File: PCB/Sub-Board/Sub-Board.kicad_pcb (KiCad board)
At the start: 4 copper layers, 50.5 x 113 mm, 200 parts, among them J1 Conn_02x08, J10 Type, J11 Power/I2C, J12 Address, J13 Power/I2C, J14 Address, J15 GPIO, J16 Type, J17 GPIO, J18 Type, J19 Power/I2C, J2 Conn_01x04_Pin, J20 Address, J21 Power/I2C, J22 Address, J23 GPIO, J24 Type, J25 GPIO, J26 Type, J27 Power/I2C, J28 Address, J29 Power/I2C, J3 Power/I2C, J30 Address, J31 GPIO, J32 Type, J33 GPIO, J34 Type, J4 Address, J5 Power/I2C, J6 Address, J7 GPIO, J8 Type, J9 GPIO, SW1 SW_DIP_x07, U1 TPS629210DRLR, U2 74HC165, U3 STM32F401VETx, U4 74HC165, U5 74HC165, U6 74HC165, U7 74HC165, Y1 26 MHz

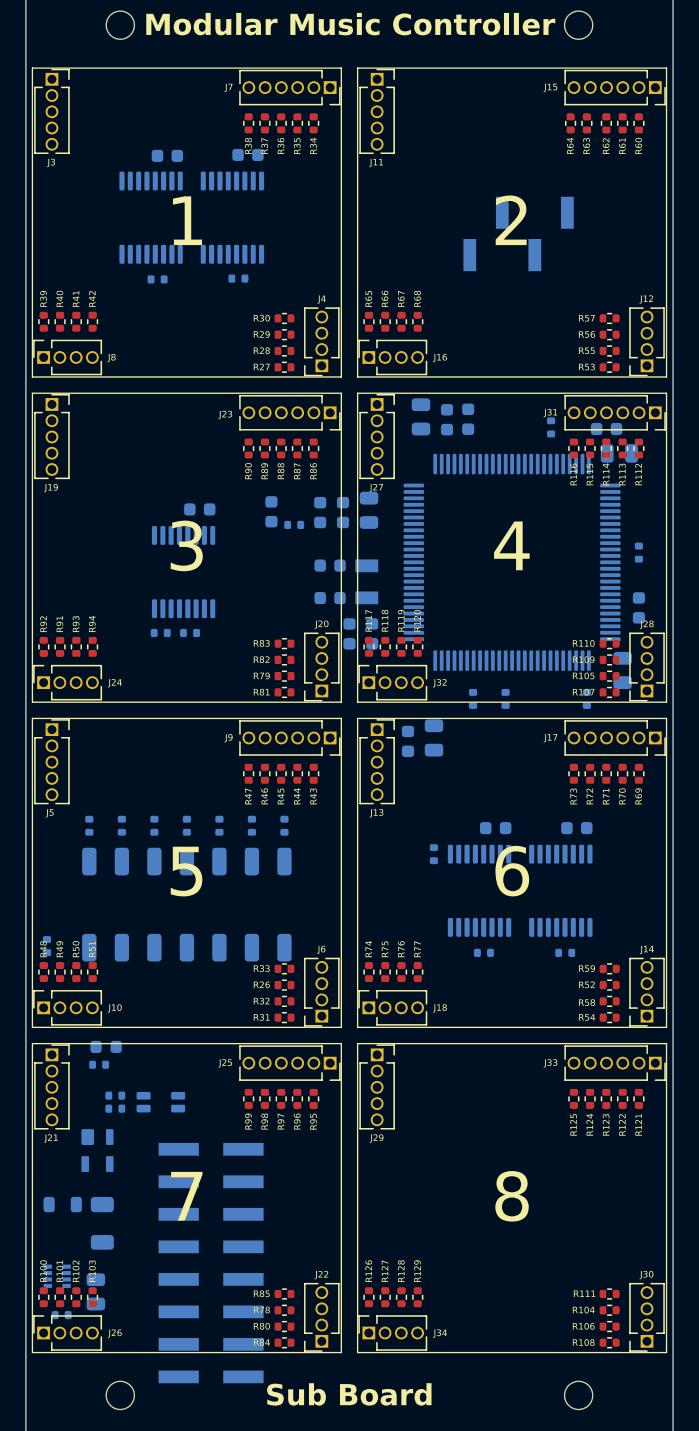
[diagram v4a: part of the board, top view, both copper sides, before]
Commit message: Sub Board PCB: Fix silkscreen size
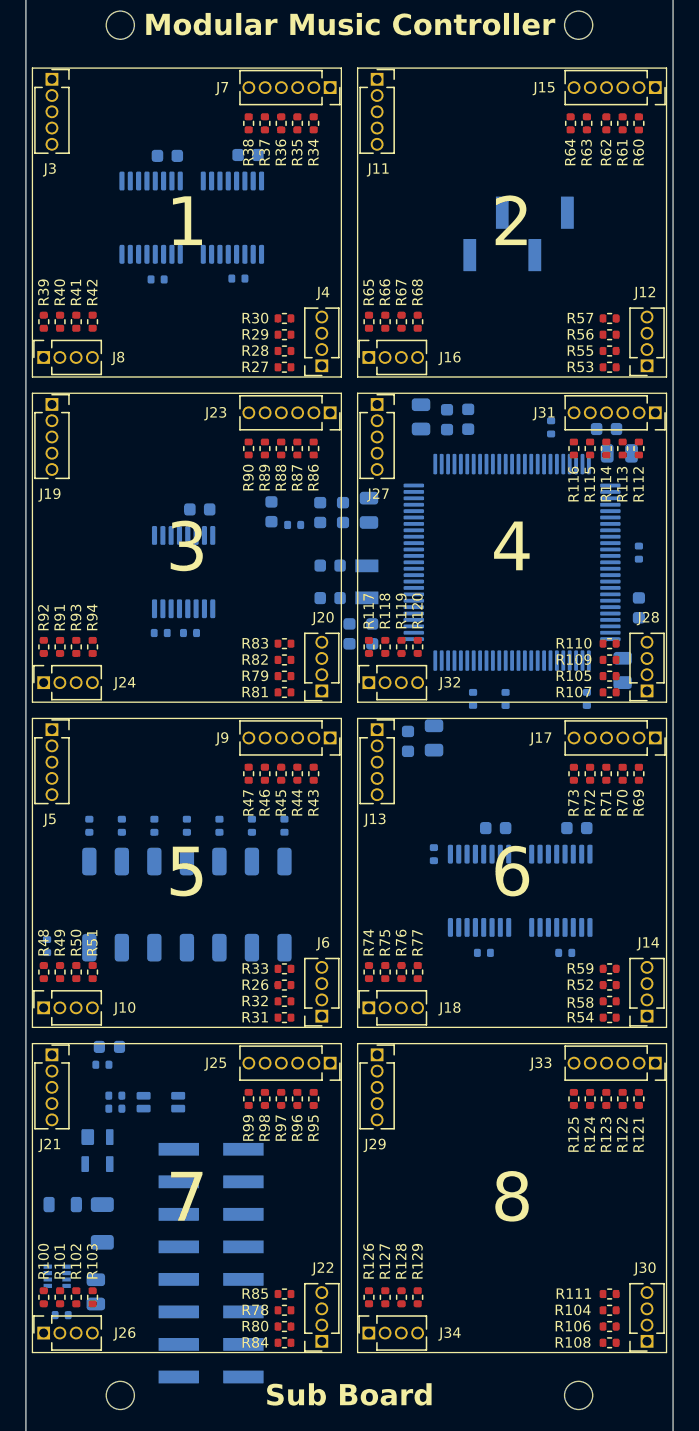
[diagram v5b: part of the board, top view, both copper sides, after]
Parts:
- moved FB1 0.26 mm to (108.2, 120.9)
- moved R4 0.26 mm to (107.7, 122.3)
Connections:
- net Net-(U1-MODE/S-CONF) renamed /Power Supply/MODE/S-CONF
- C14 pad 2: GND -> GNDD
- C17 pad 2: GND -> GNDD
- C21 pad 2: GND -> GNDD
- C24 pad 2: GND -> GNDD
- C3 pad 2: GND -> GNDD
- C4 pad 2: GND -> GNDD
- C5 pad 2: GND -> GNDD
- C6 pad 2: GND -> GNDD
- R10 pad 2: GND -> GNDD
- R100 pad 1: GND -> GNDD
- R101 pad 1: GND -> GNDD
- R102 pad 1: GND -> GNDD
- R103 pad 1: GND -> GNDD
- R109 pad 2: GND -> GNDD
- R11 pad 2: GND -> GNDD
- R110 pad 2: GND -> GNDD
- R111 pad 2: GND -> GNDD
- R112 pad 1: GND -> GNDD
- R113 pad 1: GND -> GNDD
- R114 pad 1: GND -> GNDD
- R115 pad 1: GND -> GNDD
- R116 pad 1: GND -> GNDD
- R117 pad 1: GND -> GNDD
- R118 pad 1: GND -> GNDD
- R119 pad 1: GND -> GNDD
- R12 pad 2: GND -> GNDD
- R120 pad 1: GND -> GNDD
- R121 pad 1: GND -> GNDD
- R122 pad 1: GND -> GNDD
- R123 pad 1: GND -> GNDD
- R124 pad 1: GND -> GNDD
- R125 pad 1: GND -> GNDD
- R126 pad 1: GND -> GNDD
- R127 pad 1: GND -> GNDD
- R128 pad 1: GND -> GNDD
- R129 pad 1: GND -> GNDD
- R24 pad 1: GND -> GNDD
- R27 pad 2: GND -> GNDD
- R28 pad 2: GND -> GNDD
- R29 pad 2: GND -> GNDD
- R30 pad 2: GND -> GNDD
- R31 pad 2: GND -> GNDD
- R32 pad 2: GND -> GNDD
- R33 pad 2: GND -> GNDD
- R34 pad 1: GND -> GNDD
- R35 pad 1: GND -> GNDD
- R36 pad 1: GND -> GNDD
- R37 pad 1: GND -> GNDD
- R38 pad 1: GND -> GNDD
- R39 pad 1: GND -> GNDD
- R40 pad 1: GND -> GNDD
- R41 pad 1: GND -> GNDD
- R42 pad 1: GND -> GNDD
- R43 pad 1: GND -> GNDD
- R44 pad 1: GND -> GNDD
- R45 pad 1: GND -> GNDD
- R46 pad 1: GND -> GNDD
- R47 pad 1: GND -> GNDD
- R48 pad 1: GND -> GNDD
- R49 pad 1: GND -> GNDD
- R50 pad 1: GND -> GNDD
- R51 pad 1: GND -> GNDD
- R55 pad 2: GND -> GNDD
- R56 pad 2: GND -> GNDD
- R57 pad 2: GND -> GNDD
- R58 pad 2: GND -> GNDD
- R59 pad 2: GND -> GNDD
- R6 pad 2: GND -> GNDD
- R60 pad 1: GND -> GNDD
- R61 pad 1: GND -> GNDD
- R62 pad 1: GND -> GNDD
- R63 pad 1: GND -> GNDD
- R64 pad 1: GND -> GNDD
- R65 pad 1: GND -> GNDD
- R66 pad 1: GND -> GNDD
- R67 pad 1: GND -> GNDD
- R68 pad 1: GND -> GNDD
- R69 pad 1: GND -> GNDD
- R7 pad 2: GND -> GNDD
- R70 pad 1: GND -> GNDD
- R71 pad 1: GND -> GNDD
- R72 pad 1: GND -> GNDD
- R73 pad 1: GND -> GNDD
- R74 pad 1: GND -> GNDD
- R75 pad 1: GND -> GNDD
- R76 pad 1: GND -> GNDD
- R77 pad 1: GND -> GNDD
- R8 pad 2: GND -> GNDD
- R81 pad 2: GND -> GNDD
- R82 pad 2: GND -> GNDD
- R83 pad 2: GND -> GNDD
- R84 pad 2: GND -> GNDD
- R85 pad 2: GND -> GNDD
- R86 pad 1: GND -> GNDD
- R87 pad 1: GND -> GNDD
- R88 pad 1: GND -> GNDD
- R89 pad 1: GND -> GNDD
- R9 pad 2: GND -> GNDD
- R90 pad 1: GND -> GNDD
- R91 pad 1: GND -> GNDD
- R92 pad 1: GND -> GNDD
- R93 pad 1: GND -> GNDD
- R94 pad 1: GND -> GNDD
- R95 pad 1: GND -> GNDD
- R96 pad 1: GND -> GNDD
- R97 pad 1: GND -> GNDD
- R98 pad 1: GND -> GNDD
- R99 pad 1: GND -> GNDD
- U2 pad 10: GND -> GNDD
- U2 pad 15: GND -> GNDD
- U4 pad 15: GND -> GNDD
- U5 pad 15: GND -> GNDD
- U6 pad 15: GND -> GNDD
- U7 pad 15: GND -> GNDD

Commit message: Sub Board PCB: Routing (wip)
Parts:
- moved R91 1.27 mm to (103.1, 89.7)
- moved R92 1.27 mm to (104.4, 89.7)
- moved R1 1.02 mm to (108.7, 124.7)
- moved R2 1.02 mm to (108.7, 125.7)
- turned R3 to 0 degrees
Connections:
- C14 pad 2: GNDD -> GND
- C17 pad 2: GNDD -> GND
- C21 pad 2: GNDD -> GND
- C24 pad 2: GNDD -> GND
- C3 pad 2: GNDD -> GND
- C4 pad 2: GNDD -> GND
- C5 pad 2: GNDD -> GND
- C6 pad 2: GNDD -> GND
- L1 pad 2: /STM32-MCU/SystemBus.Clock -> /STM32-MCU/SystemBus.Data
- L1 pad 3: /STM32-MCU/SystemBus.Data -> /STM32-MCU/SystemBus.Clock
- R1 pad 2: Net-(L1-Pad1) -> Net-(L1-Pad4)
- R10 pad 2: GNDD -> GND
- R100 pad 1: GNDD -> GND
- R101 pad 1: GNDD -> GND
- R102 pad 1: GNDD -> GND
- R103 pad 1: GNDD -> GND
- R109 pad 2: GNDD -> GND
- R11 pad 2: GNDD -> GND
- R110 pad 2: GNDD -> GND
- R111 pad 2: GNDD -> GND
- R112 pad 1: GNDD -> GND
- R113 pad 1: GNDD -> GND
- R114 pad 1: GNDD -> GND
- R115 pad 1: GNDD -> GND
- R116 pad 1: GNDD -> GND
- R117 pad 1: GNDD -> GND
- R118 pad 1: GNDD -> GND
- R119 pad 1: GNDD -> GND
- R12 pad 2: GNDD -> GND
- R120 pad 1: GNDD -> GND
- R121 pad 1: GNDD -> GND
- R122 pad 1: GNDD -> GND
- R123 pad 1: GNDD -> GND
- R124 pad 1: GNDD -> GND
- R125 pad 1: GNDD -> GND
- R126 pad 1: GNDD -> GND
- R127 pad 1: GNDD -> GND
- R128 pad 1: GNDD -> GND
- R129 pad 1: GNDD -> GND
- R2 pad 2: Net-(L1-Pad4) -> Net-(L1-Pad1)
- R24 pad 1: GNDD -> GND
- R27 pad 2: GNDD -> GND
- R28 pad 2: GNDD -> GND
- R29 pad 2: GNDD -> GND
- R30 pad 2: GNDD -> GND
- R31 pad 2: GNDD -> GND
- R32 pad 2: GNDD -> GND
- R33 pad 2: GNDD -> GND
- R34 pad 1: GNDD -> GND
- R35 pad 1: GNDD -> GND
- R36 pad 1: GNDD -> GND
- R37 pad 1: GNDD -> GND
- R38 pad 1: GNDD -> GND
- R39 pad 1: GNDD -> GND
- R40 pad 1: GNDD -> GND
- R41 pad 1: GNDD -> GND
- R42 pad 1: GNDD -> GND
- R43 pad 1: GNDD -> GND
- R44 pad 1: GNDD -> GND
- R45 pad 1: GNDD -> GND
- R46 pad 1: GNDD -> GND
- R47 pad 1: GNDD -> GND
- R48 pad 1: GNDD -> GND
- R49 pad 1: GNDD -> GND
- R50 pad 1: GNDD -> GND
- R51 pad 1: GNDD -> GND
- R55 pad 2: GNDD -> GND
- R56 pad 2: GNDD -> GND
- R57 pad 2: GNDD -> GND
- R58 pad 2: GNDD -> GND
- R59 pad 2: GNDD -> GND
- R6 pad 2: GNDD -> GND
- R60 pad 1: GNDD -> GND
- R61 pad 1: GNDD -> GND
- R62 pad 1: GNDD -> GND
- R63 pad 1: GNDD -> GND
- R64 pad 1: GNDD -> GND
- R65 pad 1: GNDD -> GND
- R66 pad 1: GNDD -> GND
- R67 pad 1: GNDD -> GND
- R68 pad 1: GNDD -> GND
- R69 pad 1: GNDD -> GND
- R7 pad 2: GNDD -> GND
- R70 pad 1: GNDD -> GND
- R71 pad 1: GNDD -> GND
- R72 pad 1: GNDD -> GND
- R73 pad 1: GNDD -> GND
- R74 pad 1: GNDD -> GND
- R75 pad 1: GNDD -> GND
- R76 pad 1: GNDD -> GND
- R77 pad 1: GNDD -> GND
- R8 pad 2: GNDD -> GND
- R81 pad 2: GNDD -> GND
- R82 pad 2: GNDD -> GND
- R83 pad 2: GNDD -> GND
- R84 pad 2: GNDD -> GND
- R85 pad 2: GNDD -> GND
- R86 pad 1: GNDD -> GND
- R87 pad 1: GNDD -> GND
- R88 pad 1: GNDD -> GND
- R89 pad 1: GNDD -> GND
- R9 pad 2: GNDD -> GND
- R90 pad 1: GNDD -> GND
- R91 pad 1: GNDD -> GND
- R92 pad 1: GNDD -> GND
- R93 pad 1: GNDD -> GND
- R94 pad 1: GNDD -> GND
- R95 pad 1: GNDD -> GND
- R96 pad 1: GNDD -> GND
- R97 pad 1: GNDD -> GND
- R98 pad 1: GNDD -> GND
- R99 pad 1: GNDD -> GND
- U2 pad 10: GNDD -> GND
- U2 pad 15: GNDD -> GND
- U4 pad 15: GNDD -> GND
- U5 pad 15: GNDD -> GND
- U6 pad 15: GNDD -> GND
- U7 pad 15: GNDD -> GND
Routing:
- net GND: track 0.00 -> 136.8 mm, vias 0 -> 42
- net /Board Address/+3.3V Digital: track 0.00 -> 25.8 mm, vias 0 -> 10
- net /System Bus/+5V: track 0.00 -> 16.4 mm
- net /System Bus/SystemBus-Data: track 0.00 -> 15.8 mm
- net /System Bus/SystemBus-Clock: track 0.00 -> 14.5 mm
- net /System Bus/-12V: track 0.00 -> 5.05 mm
- net /System Bus/+12V: track 0.00 -> 5.05 mm
- net Net-(U1-SW): track 0.00 -> 4.90 mm
- net /Power Supply/MODE/S-CONF: track 0.00 -> 2.65 mm
- net /STM32-MCU/Slot7.Addr2: track 0.00 -> 2.46 mm
- net /STM32-MCU/Slot7.Addr1: track 0.00 -> 2.46 mm
- net /STM32-MCU/Slot7.Addr0: track 0.00 -> 2.46 mm
- net /STM32-MCU/Slot4.Addr2: track 0.00 -> 2.46 mm
- net /STM32-MCU/Slot1.Addr2: track 0.00 -> 2.46 mm
- net /STM32-MCU/Slot1.Addr1: track 0.00 -> 2.46 mm
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
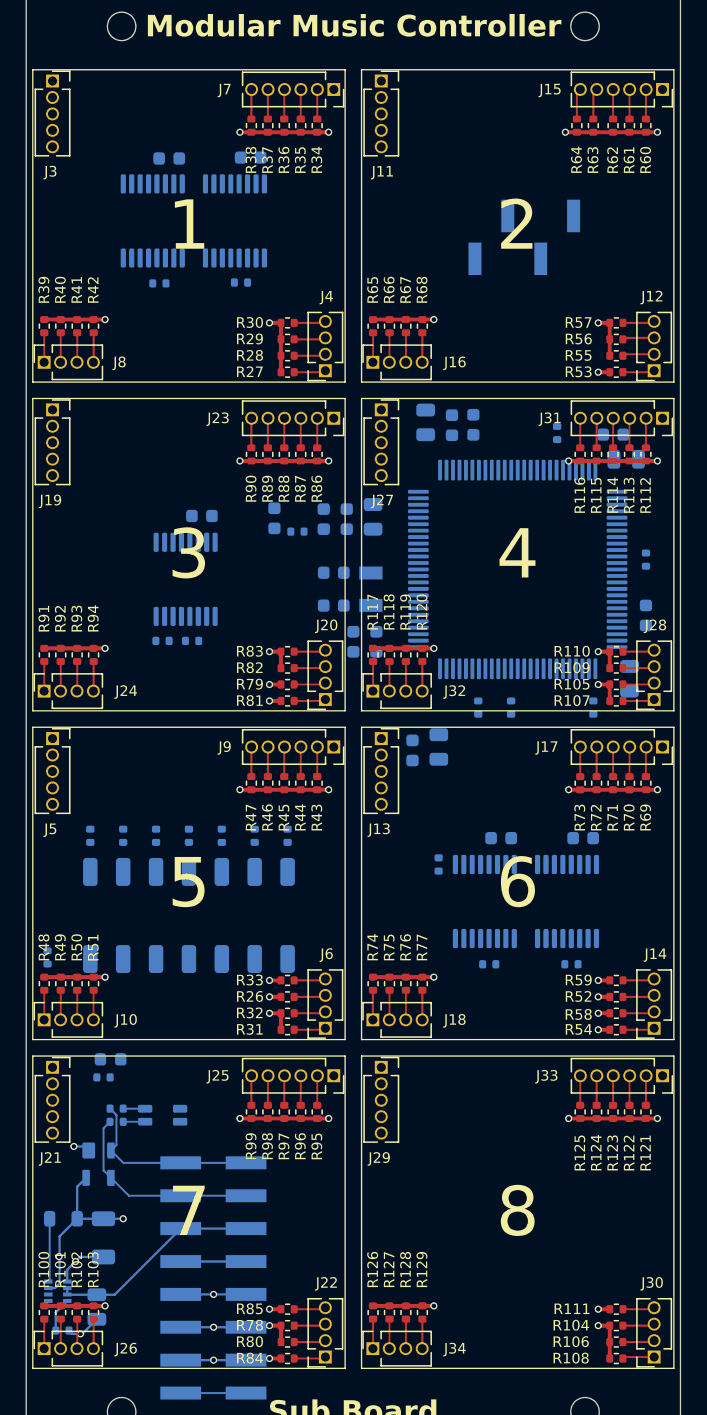
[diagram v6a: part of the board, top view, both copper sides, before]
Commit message: Sub Board PCB: Power routing
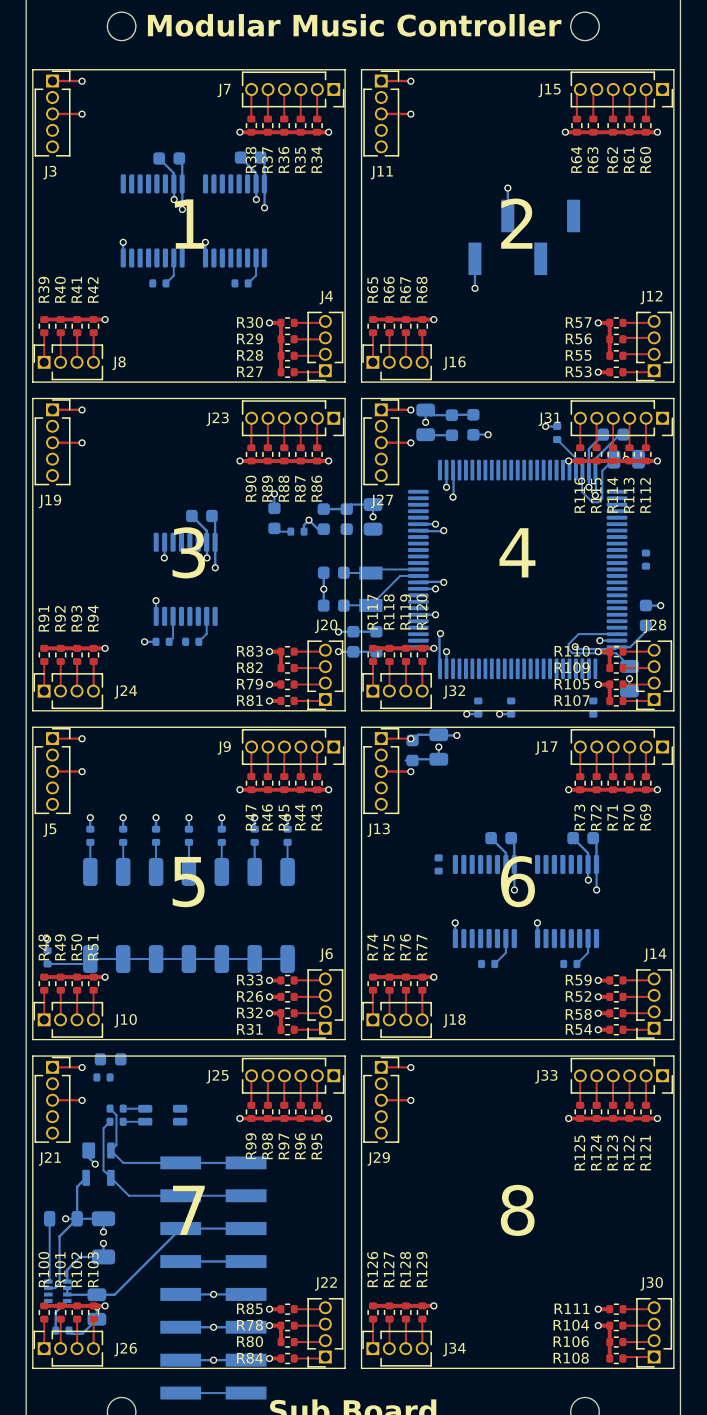
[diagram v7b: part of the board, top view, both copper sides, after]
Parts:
- moved R22 0.09 mm to (137.4, 113.5)
- moved R19 0.09 mm to (143.8, 113.5)
- moved R15 0.08 mm to (118.4, 61.0)
- moved R14 0.07 mm to (114.6, 88.6)
- moved R13 0.07 mm to (112.3, 88.6)
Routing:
- net GND: track 136.8 -> 227.4 mm, vias 42 -> 85
- net /Board Address/+3.3V Digital: track 25.8 -> 103.6 mm, vias 10 -> 39
- net Net-(R5-Pad2): track 0.00 -> 18.7 mm
- net /STM32-MCU/VCAP2: track 0.00 -> 9.78 mm
- net /STM32-MCU/VCAP1: track 0.00 -> 7.11 mm
- net /STM32-MCU/PH0: track 0.00 -> 6.71 mm
- net /STM32-MCU/PH1: track 0.00 -> 5.88 mm
- net /STM32-MCU/SlotBus.Data: track 0.00 -> 2.96 mm
- net Net-(U7-CP): track 0.00 -> 2.32 mm
- net Net-(U6-CP): track 0.00 -> 2.32 mm
- net /Board Address/BoardAddress6: track 0.00 -> 2.29 mm
- net /Board Address/BoardAddress5: track 0.00 -> 2.28 mm
- net /Board Address/BoardAddress4: track 0.00 -> 2.28 mm
- net /Board Address/BoardAddress3: track 0.00 -> 2.28 mm
- net /Board Address/BoardAddress2: track 0.00 -> 2.28 mm
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
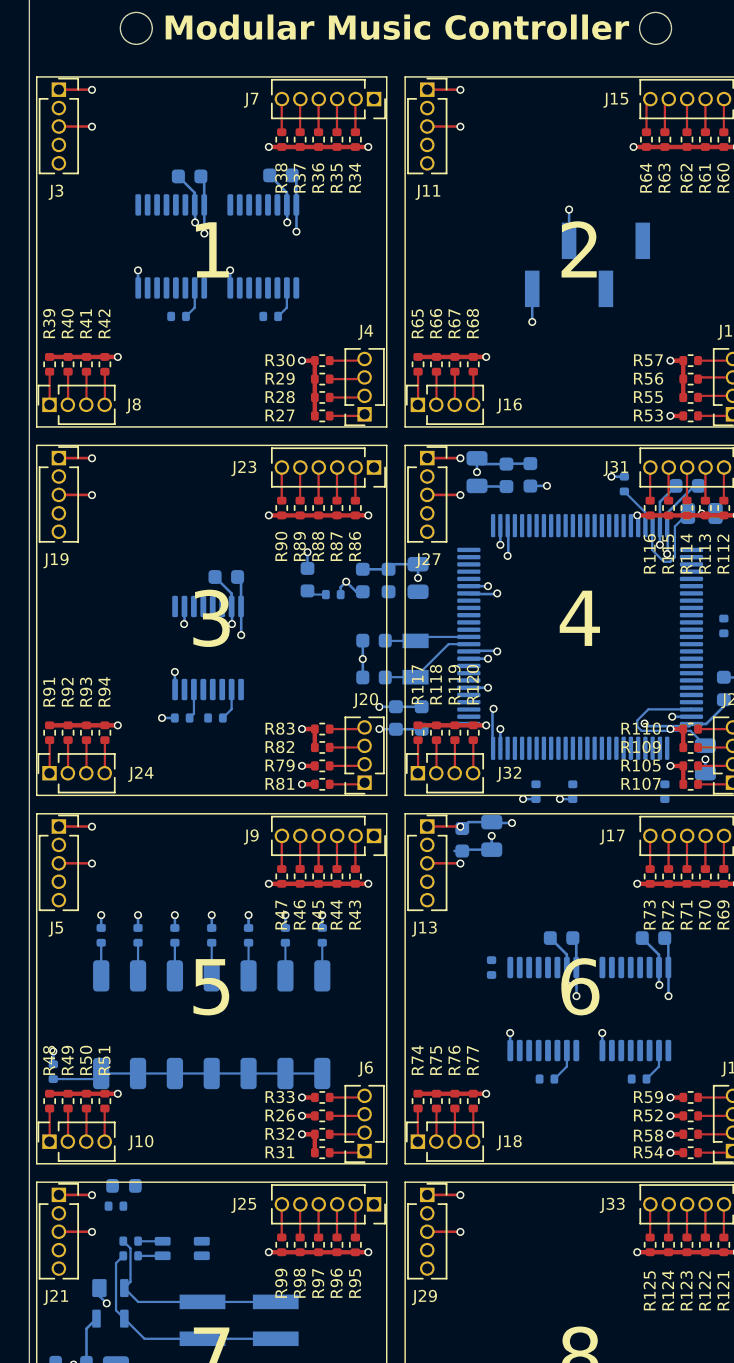
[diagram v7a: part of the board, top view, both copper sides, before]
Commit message: Sub Board PCB: Power and Slot I2C Routing
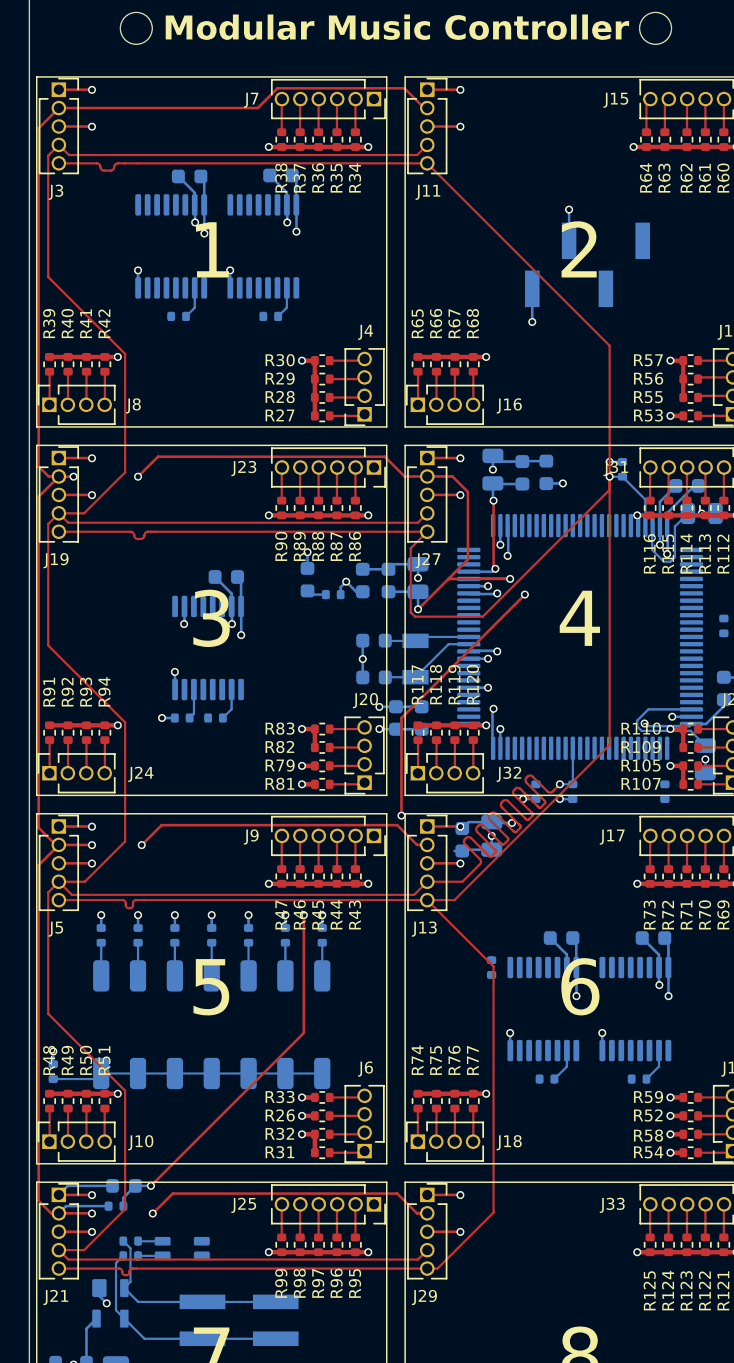
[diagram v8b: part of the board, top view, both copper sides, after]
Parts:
- moved C18 1.11 mm to (137.4, 71.7)
- moved C8 1.11 mm to (133.7, 71.5)
- moved C10 1.11 mm to (135.7, 71.7)
- moved R21 1.02 mm to (142.6, 71.5)
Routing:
- net /STM32-MCU/SlotBus.Clock: track 0.00 -> 235.1 mm, vias 0 -> 1
- net /STM32-MCU/SlotBus.Data: track 2.96 -> 225.1 mm, vias 0 -> 1
- net /Power Supply/AREF: track 0.00 -> 213.4 mm, vias 0 -> 8
- net /Power Supply/+3.3V Analog: track 2.05 -> 67.9 mm, vias 0 -> 6
- net /Board Address/+3.3V Digital: track 103.6 -> 107.6 mm
